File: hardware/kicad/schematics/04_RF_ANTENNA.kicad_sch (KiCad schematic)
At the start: 24 parts, among them J3 EXT ANT DNP

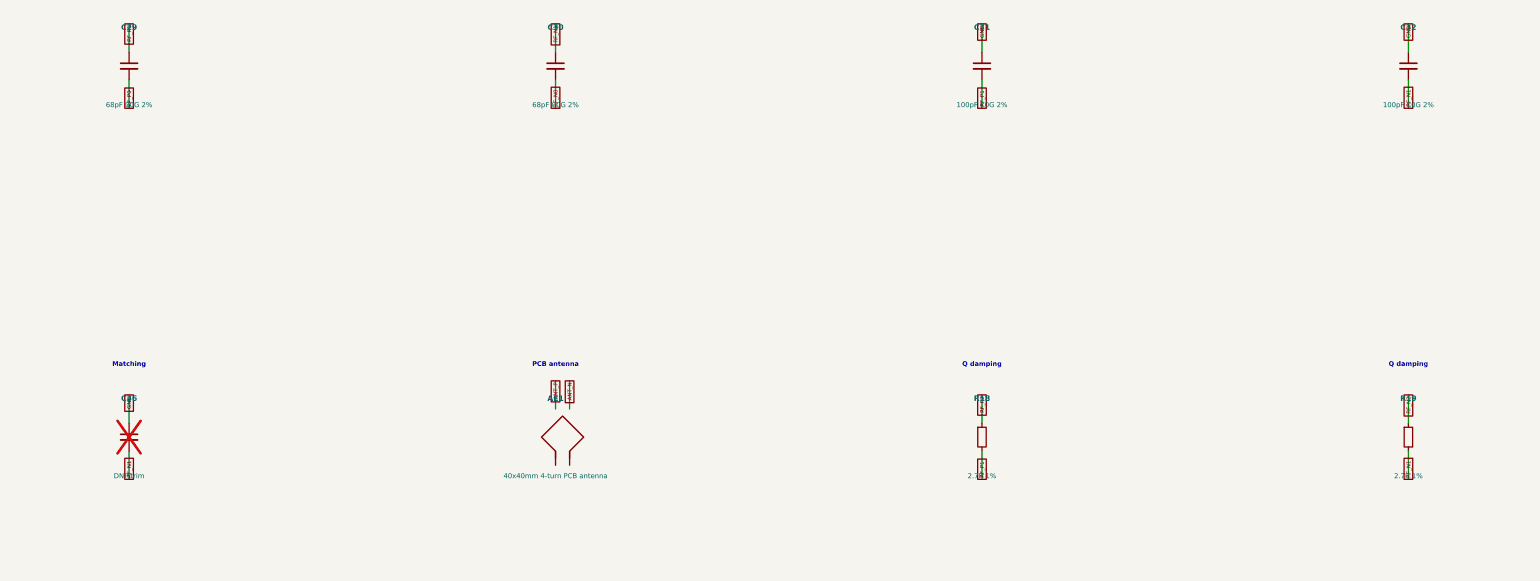
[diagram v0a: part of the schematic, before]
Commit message: Enlarge the NFC coil to 40x65 and retune the match for it
The 40x40 loop was sized by the circuit's position, not by the physics.
Coupling for a loop of radius a at range d peaks at a = d, and at a phone
tap distance of ~30-40 mm through a door leaf the 40x40 coil sat well
below that optimum while 20 mm of board west of it stayed empty.

Growing the loop to 40x65 buys about 1.74 dB of coupling and costs only
two mounting holes: H1 and H3 move from x=4 to x=53. The outline stays
150x75 and no part in the circuit moves.

Parametrise the antenna rather than retype it. AntennaSpec in
design_data.py now derives the spiral, AE1's placement, the copper
keep-out, the B.Cu underpass, the footprint's library name and AE1's
value string from one set of numbers. Four hardcoded keep-out rectangles
and a hardcoded underpass coordinate pair are gone; the underpass pair
was already wrong for any coil but 40x40, which showed up as a dangling
ANT_P track the moment the height changed. Held at height=40 the whole
parametrisation reproduces the previous board byte for byte.

Retune the matching network, which is the part that would have shipped
broken. The taller coil is 1.979 uH against 1.491, so the Rev A 68p/100p
pair resonates it at 12.11 MHz -- two bandwidths low. Both capacitors
scale by 0.75 to 51p/75p, which keeps Cp/Cs at 1.471 exactly as before,
so the impedance the PN7161 driver sees barely moves (12.75 -> 13.83 ohm,
1.7 degrees). C29/C30 become C519494 and C31/C32 become C519496, both
YAGEO NP0 +-1% 50V 0603, verified against LCSC's own product pages.

Commit the ngspice deck. PREFAB_REVIEW_ACTIONS.md quoted simulation
results the repo could not reproduce; design/sim/nfc_match.cir and
sweep.py now regenerate every number in that section. The deck lands
Rev A at 13.805 MHz rather than the 13.601 recorded earlier -- it
terminates the RX taps, which that run evidently did not -- so the
section now reports offsets against where Rev A itself lands instead of
against 13.560 absol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
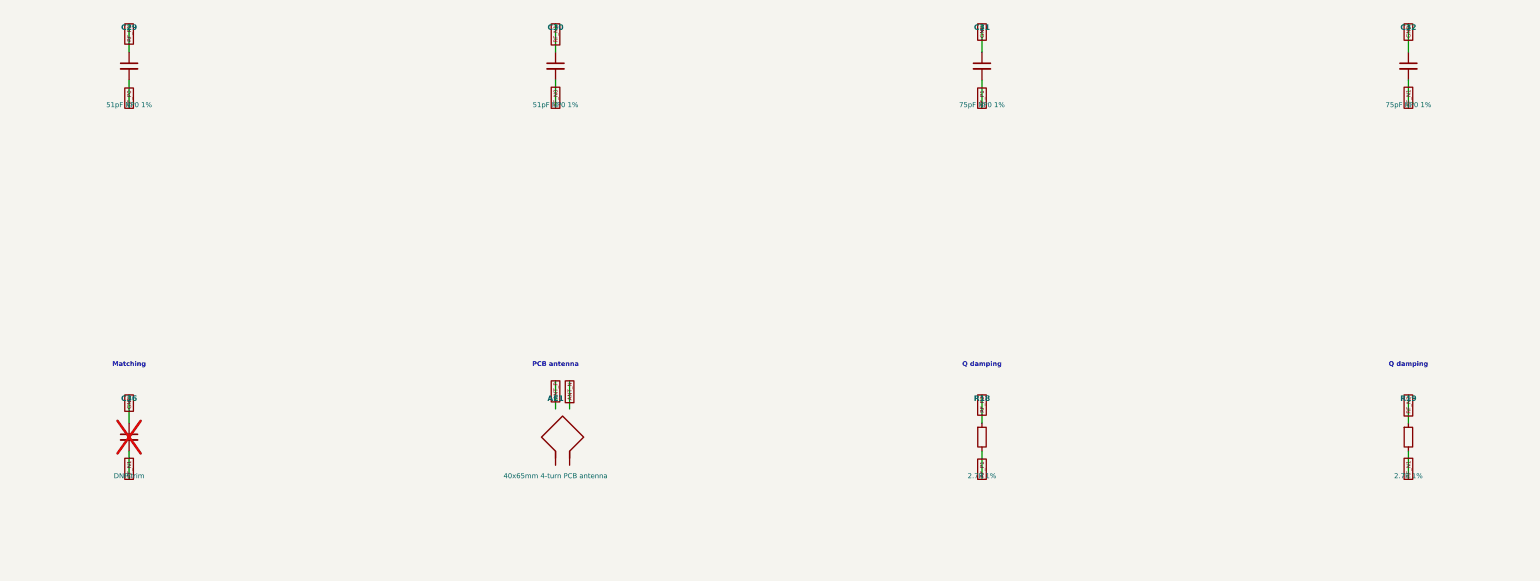
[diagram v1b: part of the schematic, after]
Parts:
- AE1: value 40x40mm 4-turn PCB antenna -> 40x65mm 4-turn PCB antenna; footprint HomeKey_RevA:NFC_Antenna_40x40_4T -> HomeKey_RevA:NFC_Antenna_40x65_4T
- C29, C30: value 68pF C0G 2% -> 51pF NP0 1%; LCSC C237335 -> C519494; MPN GRM1885C1H680FA01D -> CC0603FRNPO9BN510; Manufacturer Murata Electronics -> YAGEO
- C31, C32: value 100pF C0G 2% -> 75pF NP0 1%; LCSC C5360849 -> C519496; MPN (none) -> CC0603FRNPO9BN750; Manufacturer (none) -> YAGEO
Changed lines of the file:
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@@
       (effects (font (size 1 1) bold))
     )
-    (property "Value" "68pF C0G 2%" (id 1) (at 209 142 0)
+    (property "Value" "51pF NP0 1%" (id 1) (at 209 142 0)
       (effects (font (size 0.9 0.9)))
     )
@@
       (effects (font (size 1 1)) hide)
     )
-    (property "LCSC" "C237335" (id 4) (at 209 135 0)
-      (effects (font (size 1 1)) hide)
-    )
-    (property "MPN" "GRM1885C1H680FA01D" (id 5) (at 209 135 0)
-      (effects (font (size 1 1)) hide)
-    )
-    (property "Manufacturer" "Murata Electronics" (id 6) (at 209 135 0)
+    (property "LCSC" "C519494" (id 4) (at 209 135 0)
+      (effects (font (size 1 1)) hide)
+    )
+    (property "MPN" "CC0603FRNPO9BN510" (id 5) (at 209 135 0)
+      (effects (font (size 1 1)) hide)
+    )
+    (property "Manufacturer" "YAGEO" (id 6) (at 209 135 0)
       (effects (font (size 1 1)) hide)
     )
@@
       (effects (font (size 1 1) bold))
     )
-    (property "Value" "68pF C0G 2%" (id 1) (at 286 142 0)
+    (property "Value" "51pF NP0 1%" (id 1) (at 286 142 0)
       (effects (font (size 0.9 0.9)))
     )
@@
       (effects (font (size 1 1)) hide)
     )
-    (property "LCSC" "C237335" (id 4) (at 286 135 0)
-      (effects (font (size 1 1)) hide)
-    )
-    (property "MPN" "GRM1885C1H680FA01D" (id 5) (at 286 135 0)
-      (effects (font (size 1 1)) hide)
-    )
-    (property "Manufacturer" "Murata Electronics" (id 6) (at 286 135 0)
+    (property "LCSC" "C519494" (id 4) (at 286 135 0)
+      (effects (font (size 1 1)) hide)
+    )
+    (property "MPN" "CC0603FRNPO9BN510" (id 5) (at 286 135 0)
+      (effects (font (size 1 1)) hide)
+    )
+    (property "Manufacturer" "YAGEO" (id 6) (at 286 135 0)
       (effects (font (size 1 1)) hide)
     )
@@
       (effects (font (size 1 1) bold))
     )
-    (property "Value" "100pF C0G 2%" (id 1) (at 363 142 0)
+    (property "Value" "75pF NP0 1%" (id 1) (at 363 142 0)
       (effects (font (size 0.9 0.9)))
     )
@@
       (effects (font (size 1 1)) hide)
     )
-    (property "LCSC" "C5360849" (id 4) (at 363 135 0)
-      (effects (font (size 1 1)) hide)
-    )
-    (property "MPN" "" (id 5) (at 363 135 0)
-      (effects (font (size 1 1)) hide)
-    )
-    (property "Manufacturer" "" (id 6) (at 363 135 0)
+    (property "LCSC" "C519496" (id 4) (at 363 135 0)
+      (effects (font (size 1 1)) hide)
+    )
+    (property "MPN" "CC0603FRNPO9BN750" (id 5) (at 363 135 0)
+      (effects (font (size 1 1)) hide)
+    )
+    (property "Manufacturer" "YAGEO" (id 6) (at 363 135 0)
       (effects (font (size 1 1)) hide)
     )
@@
       (effects (font (size 1 1) bold))
     )
-    (property "Value" "100pF C0G 2%" (id 1) (at 440 142 0)
+    (property "Value" "75pF NP0 1%" (id 1) (at 440 142 0)
       (effects (font (size 0.9 0.9)))
     )
@@
       (effects (font (size 1 1)) hide)
     )
-    (property "LCSC" "C5360849" (id 4) (at 440 135 0)
-      (effects (font (size 1 1)) hide)
-    )
-    (property "MPN" "" (id 5) (at 440 135 0)
-      (effects (font (size 1 1)) hide)
-    )
-    (property "Manufacturer" "" (id 6) (at 440 135 0)
+    (property "LCSC" "C519496" (id 4) (at 440 135 0)
+      (effects (font (size 1 1)) hide)
+    )
+    (property "MPN" "CC0603FRNPO9BN750" (id 5) (at 440 135 0)
+      (effects (font (size 1 1)) hide)
+    )
+    (property "Manufacturer" "YAGEO" (id 6) (at 440 135 0)
       (effects (font (size 1 1)) hide)
     )
@@
       (effects (font (size 1 1) bold))
     )
-    (property "Value" "40x40mm 4-turn PCB antenna" (id 1) (at 286 209 0)
-      (effects (font (size 0.9 0.9)))
-    )
-    (property "Footprint" "HomeKey_RevA:NFC_Antenna_40x40_4T" (id 2) (at 286 202 0)
-      (effects (font (size 1 1)) hide)
-    )
+    (property "Value" "40x65mm 4-turn PCB antenna" (id 1) (at 286 209 0)
+      (effects (font (size 0.9 0.9)))
+    )
+    (property "Footprint" "HomeKey_RevA:NFC_Antenna_40x65_4T" (id 2) (at 286 202 0)
+      (effects (font (size 1 1)) hide)
+    )
